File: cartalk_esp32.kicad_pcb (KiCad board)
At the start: 2 copper layers, 22.9 x 48.8 mm, 22 parts, among them IC1 CP2104, J1 10118192-0002LF, Q1 mmbt2222, Q2 mmbt2222, SW2 KMR2, U1 HUB75 Connector Female, U2 AP2112-3.3, X2 ESP32_WROOM32_SKINNY

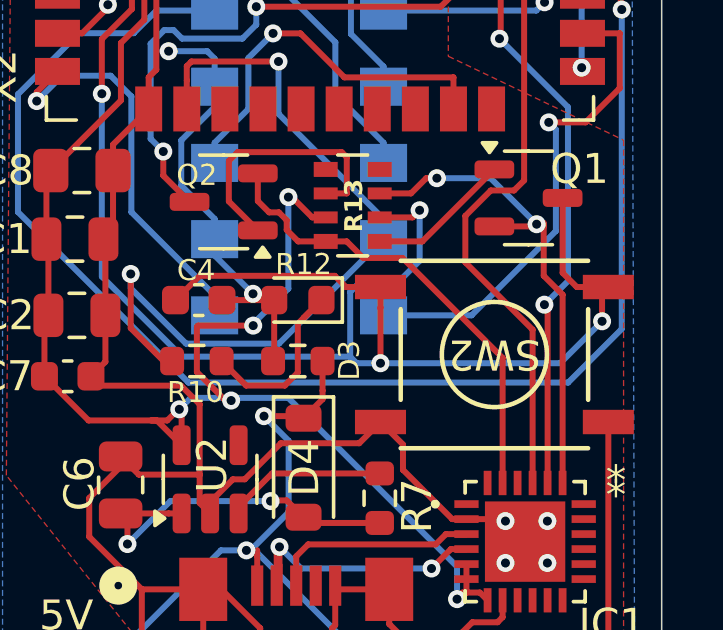
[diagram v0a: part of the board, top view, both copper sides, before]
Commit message: Add silkscreen to make HUB75 connector orientation obvious.
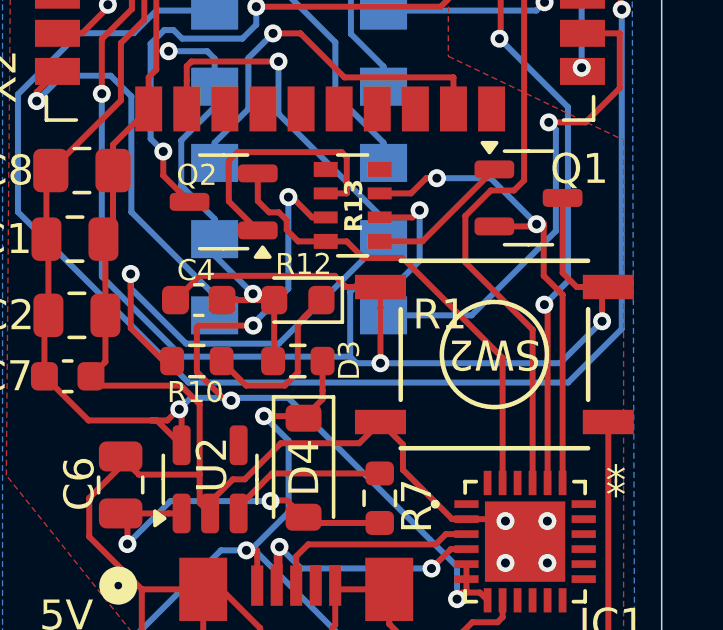
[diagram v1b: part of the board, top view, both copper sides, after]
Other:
- board text added: "R1"
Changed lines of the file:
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@@
-		)
-		(fp_line
-			(start 2.6 -0.51)
-			(end 2.6 0.51)
-			(stroke
-				(width 0.12)
-				(type solid)
-			)
-			(layer "B.SilkS")
 		)
 		(fp_line
@@
 			(pintype "input")
 		)
+	)
+	(gr_line
+		(start 133.858 103.3526)
+		(end 133.858 107.5944)
+		(stroke
+			(width 0.1)
+			(type default)
+		)
+		(layer "B.SilkS")
+	)
+	(gr_line
+		(start 133.858 107.5944)
+		(end 132.9436 107.5944)
+		(stroke
+			(width 0.1)
+			(type default)
+		)
+		(layer "B.SilkS")
+	)
+	(gr_line
+		(start 132.9944 103.3526)
+		(end 133.858 103.3526)
+		(stroke
+			(width 0.1)
+			(type default)
+		)
+		(layer "B.SilkS")
 	)
 	(gr_line
@@
 			)
 			(justify left bottom)
+		)
+	)
+	(gr_text "R1"
+		(at 132.6642 114.8588 0)
+		(layer "F.SilkS")
+		(effects
+			(font
+				(size 1 1)
+				(thickness 0.1)
+			)
+			(justify left bottom)

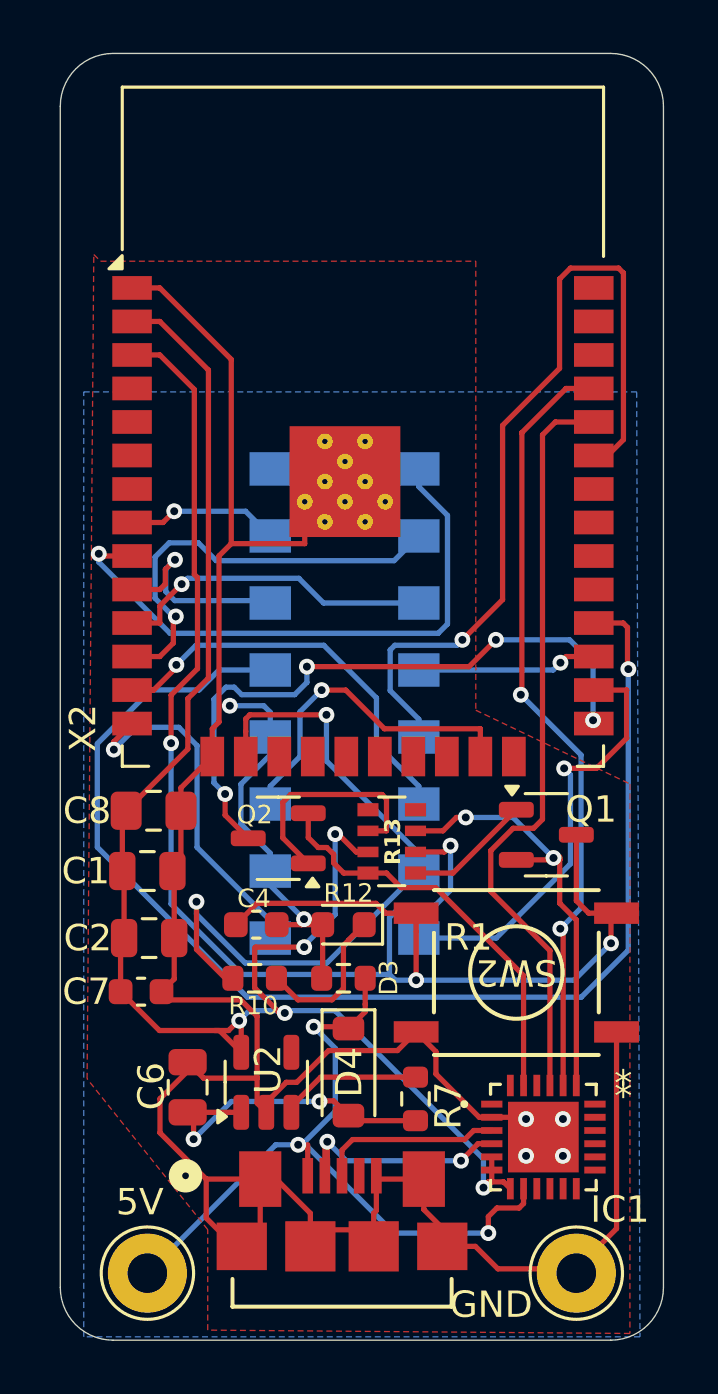
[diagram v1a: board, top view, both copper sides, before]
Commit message: Increase track width on VBUS on B.Cu.
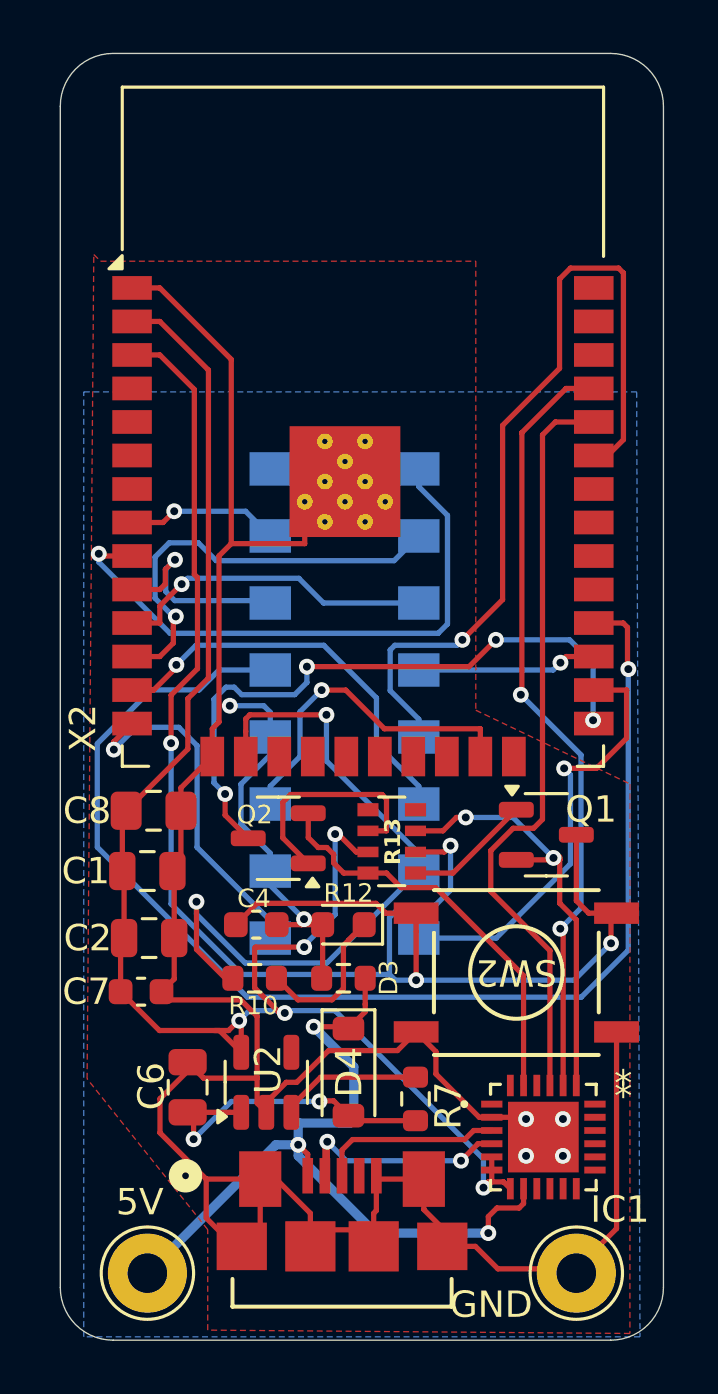
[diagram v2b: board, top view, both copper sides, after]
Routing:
- net VBUS: track 29.9 -> 31.9 mm
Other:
- board text removed: "R1"
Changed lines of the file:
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@@
 			(outputformat 1)
 			(mirror no)
-			(drillshape 1)
+			(drillshape 0)
 			(scaleselection 1)
-			(outputdirectory "")
+			(outputdirectory "manufacturing/")
 		)
 	)
@@
 			(size 1.175 1.45)
 			(layers "F.Cu" "F.Paste" "F.Mask")
-			(roundrect_rratio 0.212766)
+			(roundrect_rratio 0.2127659574)
 			(net 2 "3.3V")
 			(pinfunction "1")
@@
 			(size 1.175 1.45)
 			(layers "F.Cu" "F.Paste" "F.Mask")
-			(roundrect_rratio 0.212766)
+			(roundrect_rratio 0.2127659574)
 			(net 1 "GND")
 			(pinfunction "2")
@@
 	)
 	(gr_text "5V"
-		(at 124.9934 128.27 0)
+		(at 125.0188 128.3462 0)
 		(layer "B.SilkS")
 		(effects
@@
 		)
 	)
-	(gr_text "R1"
-		(at 132.6642 114.8588 0)
-		(layer "F.SilkS")
-		(effects
-			(font
-				(size 1 1)
-				(thickness 0.1)
-			)
-			(justify left bottom)
-		)
-	)
 	(gr_text "5V"
 		(at 120.2182 124.8918 0)
@@
 	)
 	(segment
-		(start 127.375 96.2375)
-		(end 127.1557 96.4568)
-		(width 0.2)
-		(layer "B.Cu")
-		(net 1)
-	)
-	(segment
-		(start 126.069 96.52)
-		(end 127.1557 96.52)
-		(width 0.2)
-		(layer "B.Cu")
-		(net 1)
-	)
-	(segment
 		(start 126.069 111.76)
 		(end 126.069 111.0868)
@@
 	)
 	(segment
-		(start 127.1557 96.4568)
-		(end 127.1557 96.52)
+		(start 126.069 107.3532)
+		(end 126.069 106.68)
 		(width 0.2)
 		(layer "B.Cu")
@@
 	)
 	(segment
-		(start 126.069 107.3532)
-		(end 126.069 106.68)
+		(start 125.8205 105.4948)
+		(end 126.069 105.7433)
 		(width 0.2)
 		(layer "B.Cu")
@@
 	)
 	(segment
-		(start 125.8205 105.4948)
-		(end 126.069 105.7433)
+		(start 126.069 96.52)
+		(end 127.6096 96.52)
 		(width 0.2)
 		(layer "B.Cu")
@@
 	)
 	(segment
+		(start 127.488 122.4951)
+		(end 127.127 122.1341)
+		(width 0.2)
+		(layer "F.Cu")
+		(net 12)
+	)
+	(segment
 		(start 134.333 125.227)
 		(end 134.333 124.856)
@@
 	)
 	(segment
-		(start 127.3125 122.232)
-		(end 127.2146 122.1341)
-		(width 0.2)
-		(layer "F.Cu")
-		(net 12)
-	)
-	(segment
 		(start 127.488 123.309)
-		(end 127.488 122.334)
+		(end 127.488 122.4951)
 		(width 0.2)
 		(layer "F.Cu")
@@
 	)
 	(segment
-		(start 127.488 122.334)
-		(end 127.488 122.132)
-		(width 0.2)
-		(layer "F.Cu")
-		(net 12)
-	)
-	(segment
 		(start 135.499 124.531)
 		(end 135.668 124.362)
@@
 	)
 	(segment
-		(start 127.4104 122.1341)
-		(end 130.7576 125.4813)
-		(width 0.2)
+		(start 127.127 121.3612)
+		(end 127.127 122.1341)
+		(width 0.35)
 		(layer "B.Cu")
 		(net 12)
 	)
 	(segment
-		(start 130.7576 125.4813)
-		(end 134.3331 125.4813)
-		(width 0.2)
+		(start 129.2352 119.5832)
+		(end 129.2352 119.1817)
+		(width 0.35)
 		(layer "B.Cu")
 		(net 12)
 	)
 	(segment
-		(start 128.5342 118.4807)
+		(start 129.2352 119.1817)
 		(end 127.7137 117.6602)
-		(width 0.2)
+		(width 0.35)
+		(layer "B.Cu")
+		(net 12)
+	)
+	(segment
+		(start 127.127 122.1341)
+		(end 127.127 122.555)
+		(width 0.35)
 		(layer "B.Cu")
 		(net 12)
@@
 		(start 126.2779 122.1341)
 		(end 121.412 127)
-		(width 0.2)
+		(width 0.35)
 		(layer "B.Cu")
 		(net 12)
@@
 		(start 127.127 122.1341)
 		(end 126.2779 122.1341)
-		(width 0.2)
+		(width 0.35)
+		(layer "B.Cu")
+		(net 12)
+	)
+	(segment
+		(start 129.2352 121.1834)
+		(end 129.1082 121.3104)
+		(width 0.35)
+		(layer "B.Cu")
+		(net 12)
+	)
+	(segment
+		(start 129.2352 119.5832)
+		(end 129.2352 121.1834)
+		(width 0.35)
+		(layer "B.Cu")
+		(net 12)
+	)
+	(segment
+		(start 127.1778 121.3104)
+		(end 127.127 121.3612)
+		(width 0.35)
 		(layer "B.Cu")
 		(net 12)
@@
 		(start 127.127 122.1341)
 		(end 127.2642 122.1341)
-		(width 0.2)
+		(width 0.35)
 		(layer "B.Cu")
 		(net 12)
 	)
 	(segment
-		(start 127.127 122.1341)
-		(end 127.4104 122.1341)
-		(width 0.2)
+		(start 130.0533 125.4813)
+		(end 134.3331 125.4813)
+		(width 0.35)
 		(layer "B.Cu")
 		(net 12)
 	)
 	(segment
-		(start 128.5342 120.8641)
-		(end 128.5342 118.4807)
-		(width 0.2)
+		(start 129.1082 121.3104)
+		(end 127.1778 121.3104)
+		(width 0.35)
 		(layer "B.Cu")
 		(net 12)
 	)
 	(segment
-		(start 127.2642 122.1341)
-		(end 128.5342 120.8641)
-		(width 0.2)
+		(start 127.127 122.555)
+		(end 130.0533 125.4813)
+		(width 0.35)
 		(layer "B.Cu")
 		(net 12)
